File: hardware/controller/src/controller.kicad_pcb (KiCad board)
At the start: 2 copper layers, 85 x 35 mm, 32 parts, among them J1 To Display, J2 Display, J3 Barrel_Jack_Switch, J4 Program, J5 JTAG, SW1 RESET, SW2 BTN1, SW3 BTN1, U1 ESP32-WROOM-32D, U2 XL1509-5.0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

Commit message: Changed micro symbol to uF
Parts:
- C2: value 100µF -> 10uF
- C3: value 1µF -> 100nF
- C4, C7: value 22µF -> 22uF
- C6, C9: value 100µF -> 100uF
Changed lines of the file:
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@@
 			)
 		)
-		(property "Value" "22µF"
+		(property "Value" "22uF"
 			(at 0 3.7 90)
 			(layer "F.Fab")
@@
 			)
 		)
-		(property "Value" "100µF"
+		(property "Value" "10uF"
 			(at 0 1.68 90)
 			(layer "F.Fab")
@@
 			)
 		)
-		(property "Value" "22µF"
+		(property "Value" "22uF"
 			(at 0 3.7 90)
 			(layer "F.Fab")
@@
 			)
 		)
-		(property "Value" "100µF"
+		(property "Value" "100uF"
 			(at 0 2.35 90)
 			(layer "F.Fab")
@@
 			)
 		)
-		(property "Value" "1µF"
+		(property "Value" "100nF"
 			(at 0 1.68 90)
 			(layer "F.Fab")
@@
 			)
 		)
-		(property "Value" "100µF"
+		(property "Value" "100uF"
 			(at 0 2.35 90)
 			(layer "F.Fab")

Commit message: Changed micro symbol to uF
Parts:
- L1: value 68µH -> 68uH
- L2: value 47µH -> 47uH
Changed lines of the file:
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@@
 			)
 		)
-		(property "LCSC" "C61063"
+		(property "LCSC" "C2681226"
 			(at 0 0 180)
 			(unlocked yes)
@@
 			)
 		)
-		(property "Value" "47µH"
+		(property "Value" "47uH"
 			(at 0 4 90)
 			(layer "F.Fab")
@@
 			)
 		)
-		(property "Value" "68µH"
+		(property "Value" "68uH"
 			(at 0 4 90)
 			(layer "F.Fab")

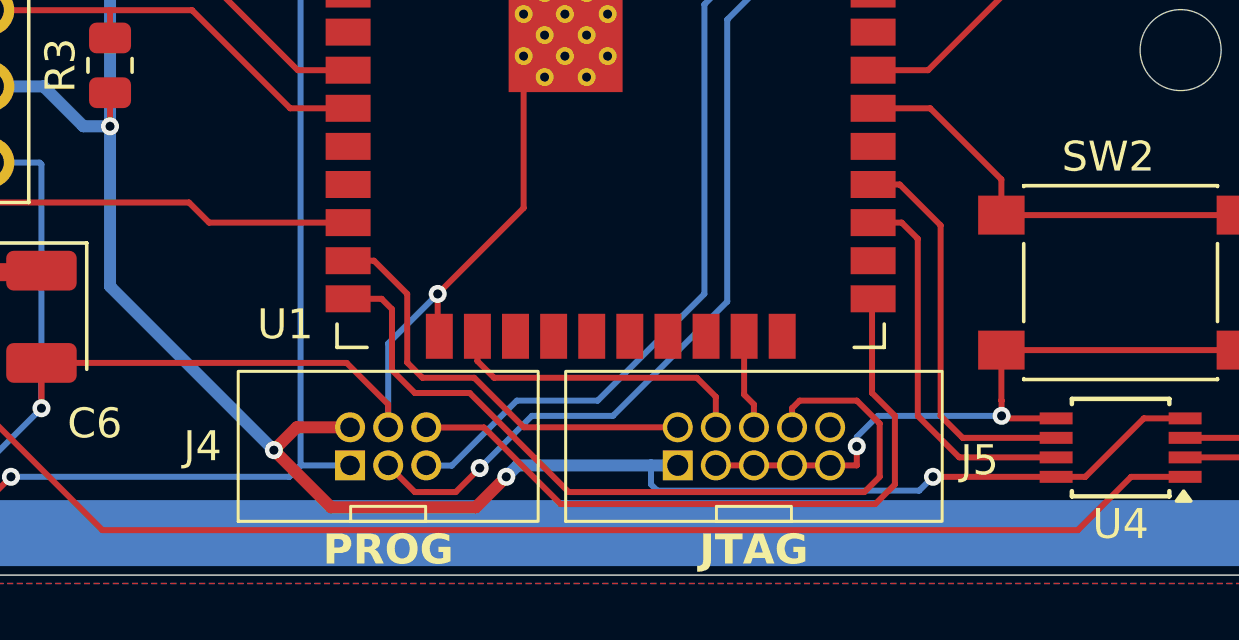
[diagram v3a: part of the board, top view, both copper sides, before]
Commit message: Added some testpads
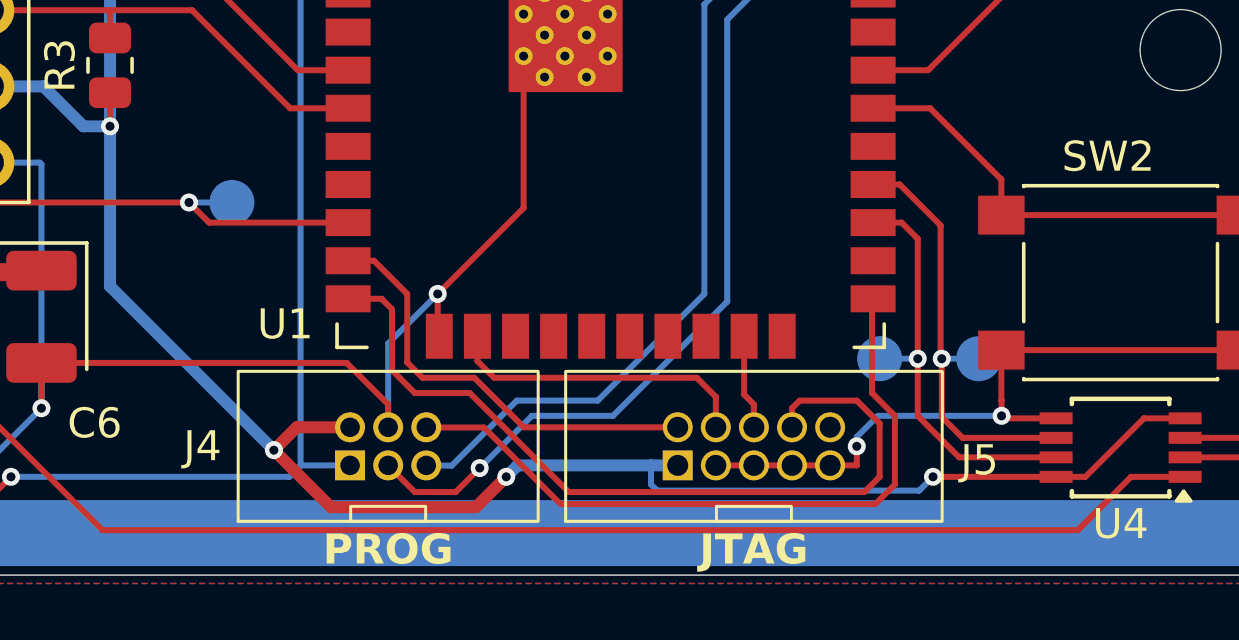
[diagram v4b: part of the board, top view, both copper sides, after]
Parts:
- added TP1: ~, TestPoint:TestPoint_Pad_D1.5mm, B.Cu at (136.1, 108.6)
- added TP2: ~, TestPoint:TestPoint_Pad_D1.5mm, B.Cu at (139.4, 108.6)
- added TP3: ~, TestPoint:TestPoint_Pad_D1.5mm, B.Cu at (114.5, 103.4)
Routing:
- net /WLED: track 29.7 -> 31.2 mm, vias 0 -> 1
- net /UART1_RX: track 12.8 -> 14.1 mm, vias 0 -> 1
- net /UART1_TX: track 13.3 -> 14.5 mm, vias 0 -> 1

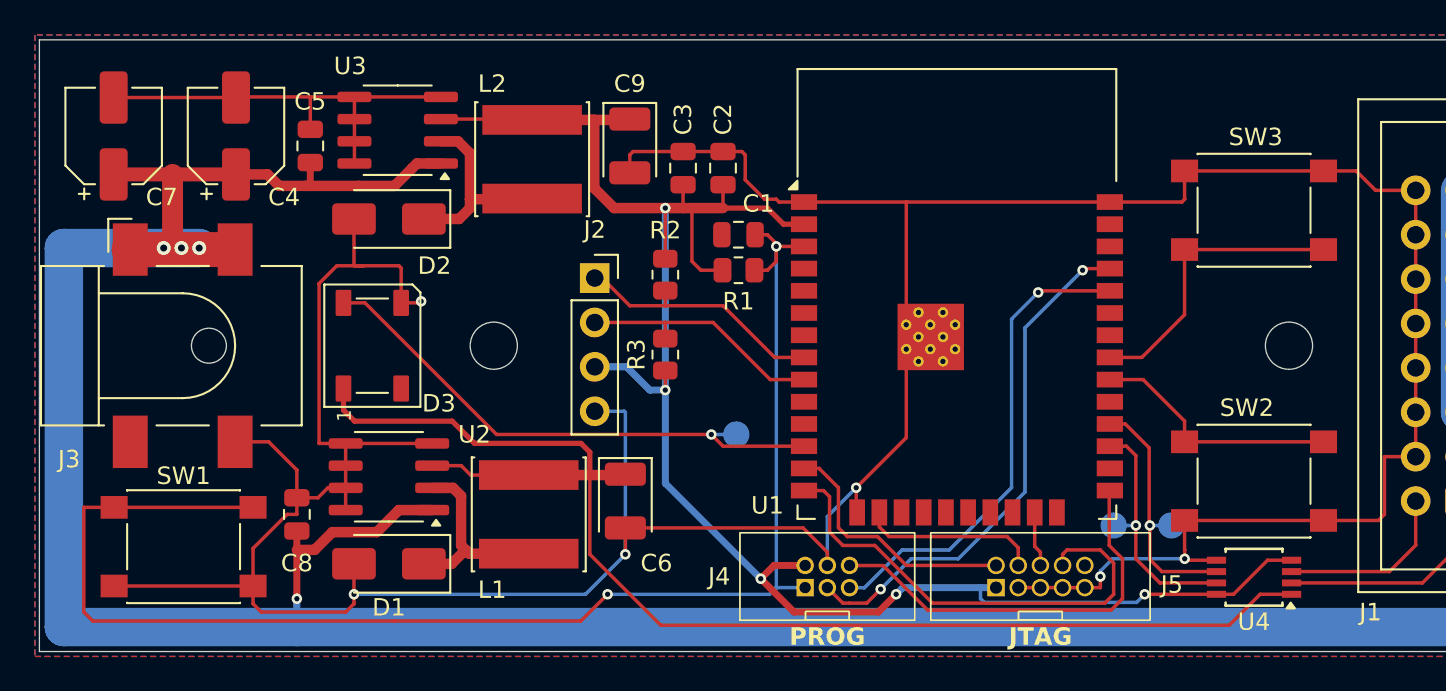
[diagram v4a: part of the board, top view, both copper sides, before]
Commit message: added blender renderes to kibot
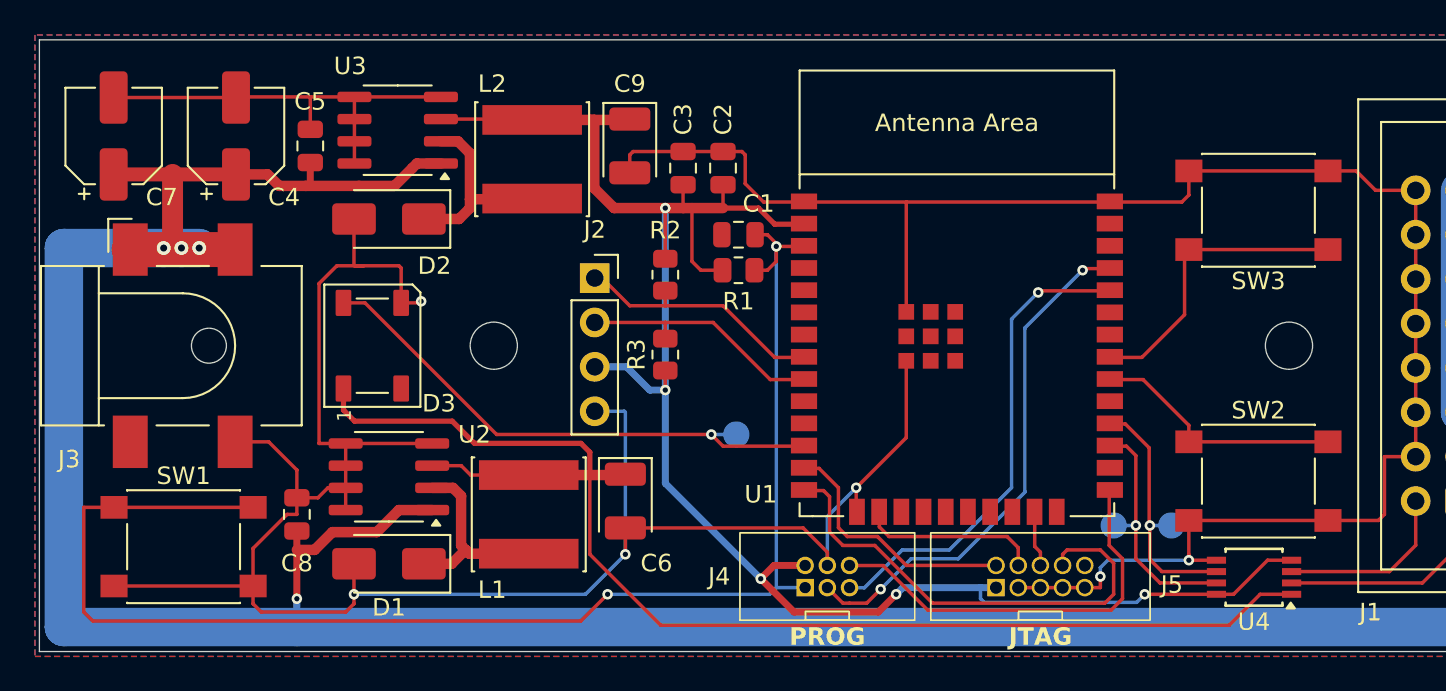
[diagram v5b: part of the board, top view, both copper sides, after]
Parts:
- SW1, SW2, SW3: footprint Button_Switch_SMD:SW_Push_1P1T_NO_6x6mm_H9.5mm -> Button_Switch_SMD:SW_SPST_PTS645
- U1: value ESP32-WROOM-32D -> ESP32-WROOM-E; footprint RF_Module:ESP32-WROOM-32D -> PCM_Espressif:ESP32-WROOM-32E
- moved U1 1.27 mm to (127.1, 97.1)
- moved SW2 0.25 mm to (144.3, 106.1)
- moved SW3 0.25 mm to (144.3, 90.6)
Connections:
- U1 pad 17: unconnected-(U1-SHD/SD2-Pad17) -> (no net)
- U1 pad 18: unconnected-(U1-SWP/SD3-Pad18) -> (no net)
- U1 pad 19: unconnected-(U1-SCS/CMD-Pad19) -> (no net)
- U1 pad 20: unconnected-(U1-SCK/CLK-Pad20) -> (no net)
- U1 pad 21: unconnected-(U1-SDO/SD0-Pad21) -> (no net)
- U1 pad 22: unconnected-(U1-SDI/SD1-Pad22) -> (no net)
- U1 pad 32: unconnected-(U1-NC-Pad32) -> (no net)
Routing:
- net GND: track 247.4 -> 247.9 mm

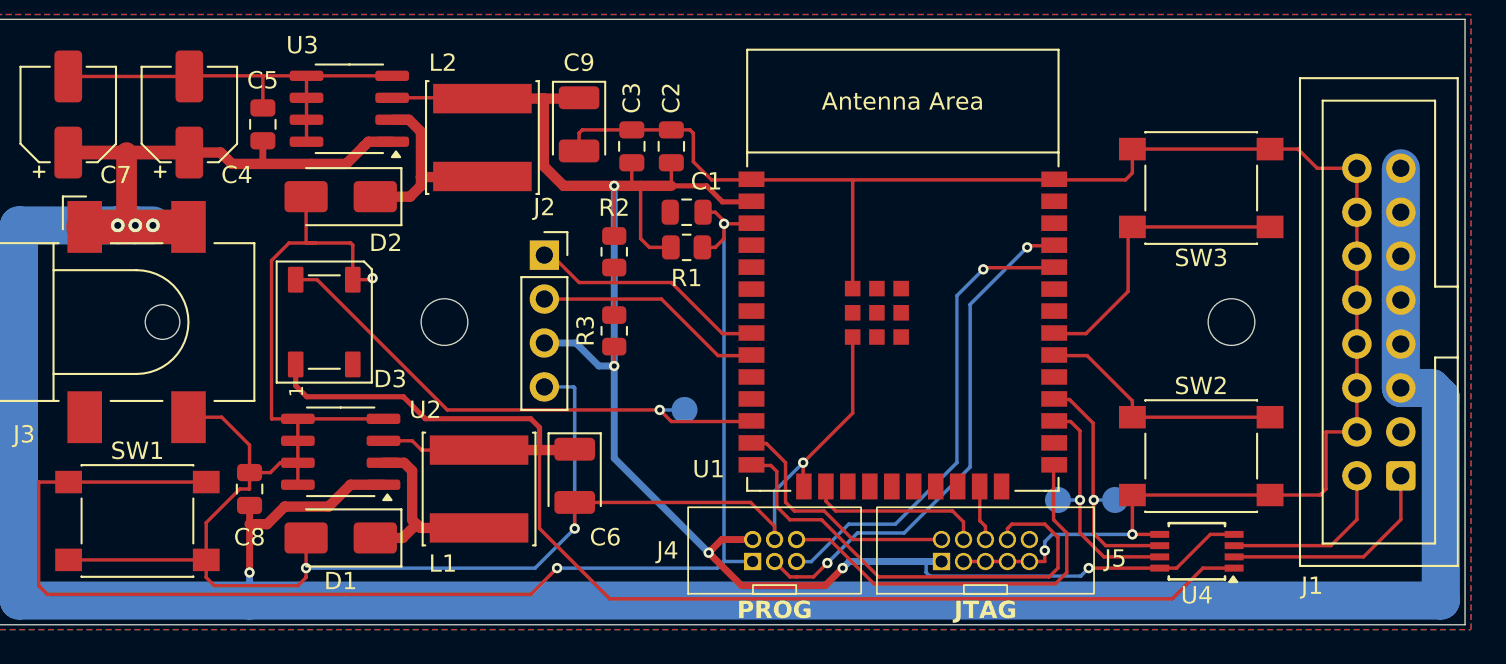
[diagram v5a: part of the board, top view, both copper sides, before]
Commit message: Updated controller footprint and added testpads
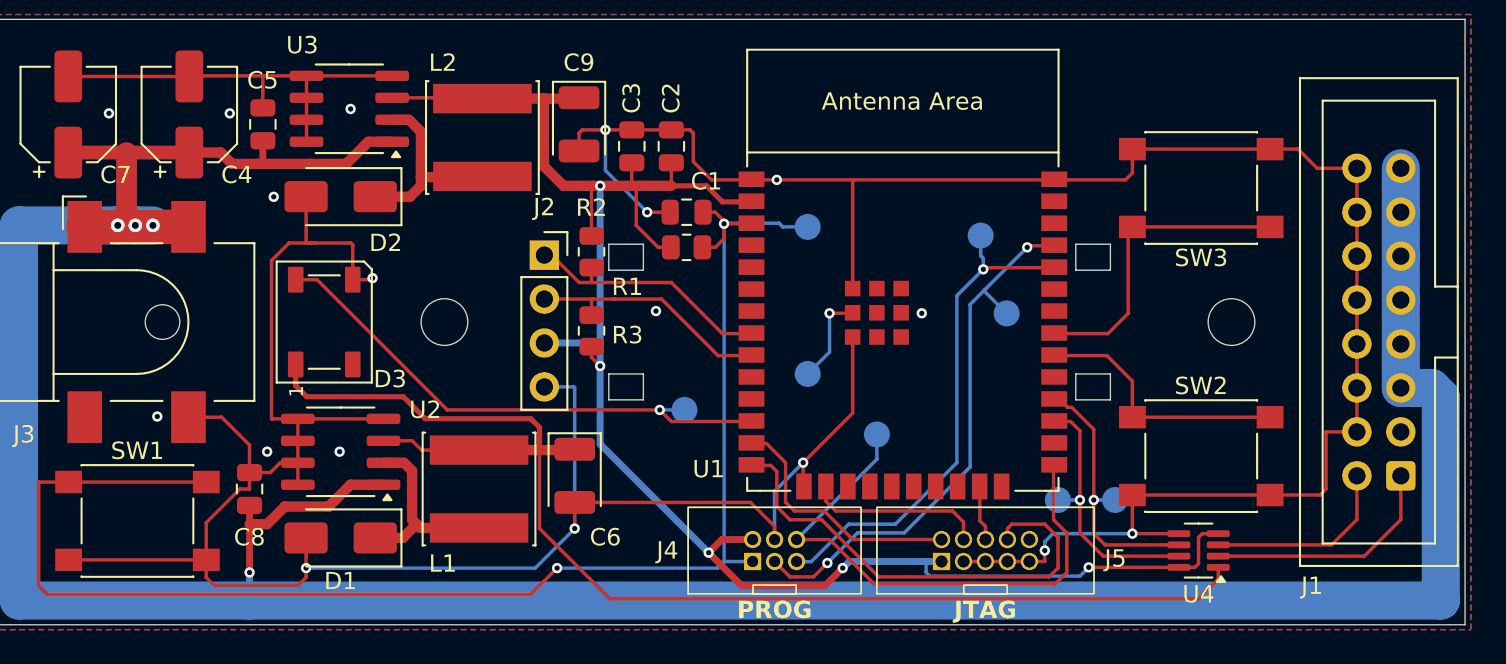
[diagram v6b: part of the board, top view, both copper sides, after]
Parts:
- added TP4: ~, TestPoint:TestPoint_Pad_D1.5mm, B.Cu at (133.1, 97.8)
- added TP5: ~, TestPoint:TestPoint_Pad_D1.5mm, B.Cu at (131.6, 93.3)
- added TP6: ~, TestPoint:TestPoint_Pad_D1.5mm, B.Cu at (121.6, 92.8)
- added TP7: ~, TestPoint:TestPoint_Pad_D1.5mm, B.Cu at (125.6, 104.8)
- added TP8: ~, TestPoint:TestPoint_Pad_D1.5mm, B.Cu at (121.6, 101.3)
- U4: footprint Package_SO:TSSOP-8_3x3mm_P0.65mm -> Package_TO_SOT_SMD:SOT-23-8
- moved R2 1.31 mm to (109.1, 94.3)
- moved R3 1.31 mm to (109.1, 98.9)
- moved U4 0.10 mm to (144.2, 111.6)
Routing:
- net GND: track 247.9 -> 261.5 mm, vias 6 -> 19
- net /IO0: track 23.5 -> 31.5 mm
- net /EN: track 83.2 -> 88.2 mm
- net /UART0_RX: track 27.7 -> 29.7 mm
- net /UART0_TX: track 30.0 -> 31.8 mm
- net /UART1_RX: track 14.1 -> 15.2 mm
- net /UART1_TX: track 14.5 -> 15.5 mm
- net /UART1_TX_M: track 10.3 -> 11.2 mm
- net /UART1_RX_M: track 13.1 -> 14.0 mm
- net +3V3: track 104.7 -> 103.9 mm
- net /BTN2: track 17.0 -> 17.7 mm
- net /BTN1: track 14.5 -> 15.2 mm
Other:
- outline, holes or cut-outs redrawn

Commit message: connect dc jack ground pin
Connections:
- J3 pad 3: unconnected-(J3-Pad3) -> GND

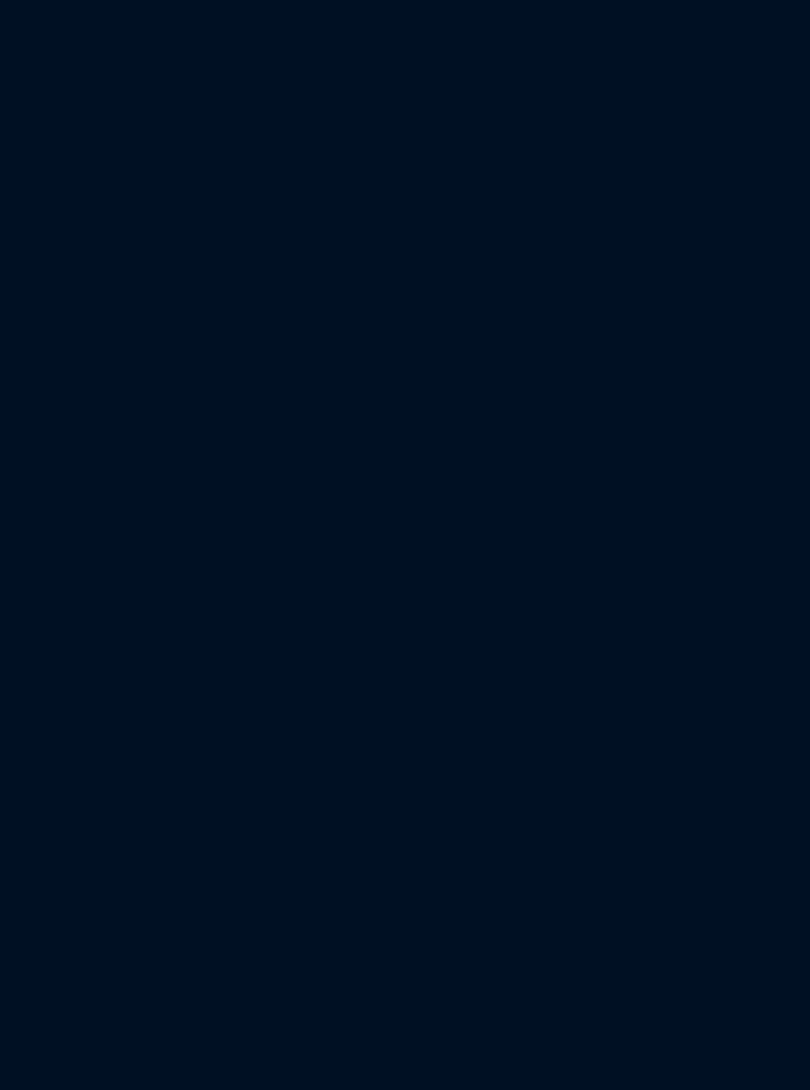
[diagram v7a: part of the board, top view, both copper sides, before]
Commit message: Update side panel to add proper ESD protection, 12V detection, removed uart switch in favor of software switching, shuffled around some IO for improved routing.
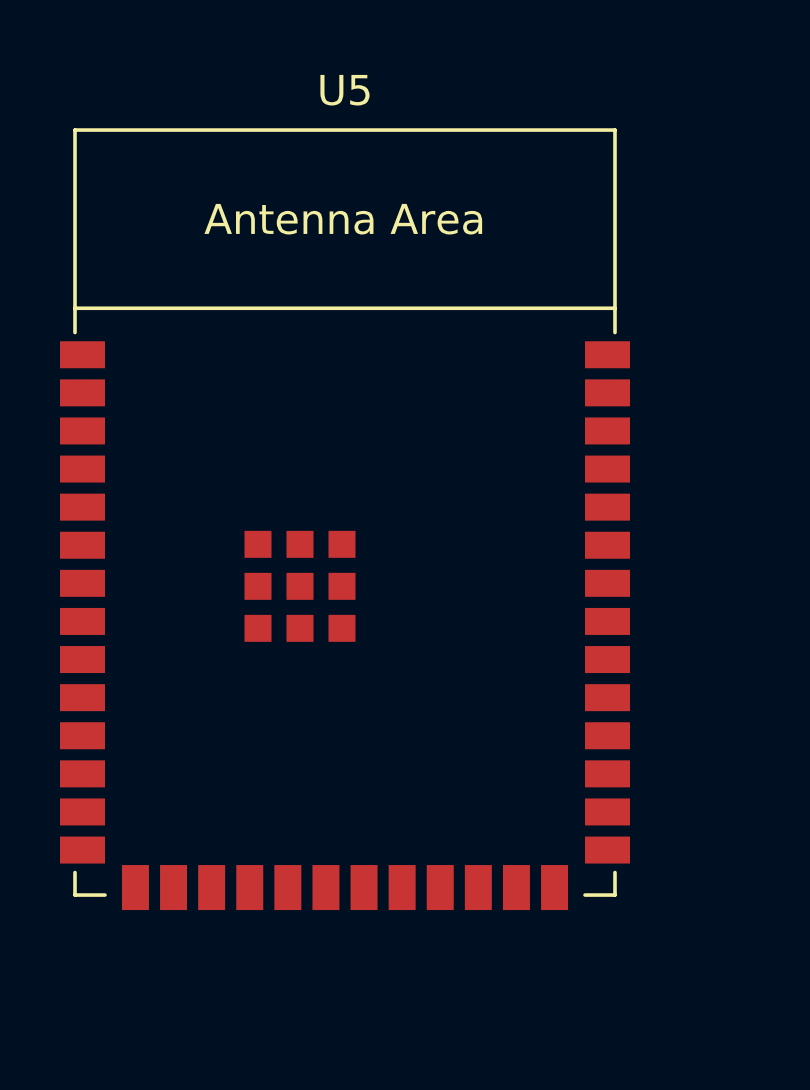
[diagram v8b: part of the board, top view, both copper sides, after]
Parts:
- added U5: ESP32-S3-WROOM-1, PCM_Espressif:ESP32-S3-WROOM-1, F.Cu at (42.2, 77.7)
